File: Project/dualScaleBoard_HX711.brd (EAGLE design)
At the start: 75 x 14 mm, 44 parts, among them Q1 MMBT4403, Q2 MMBT4403, U1 HX711, U2 HX711

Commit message: BOM update
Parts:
- R7: value 20K -> 20k
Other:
- outline, holes or cut-outs redrawn

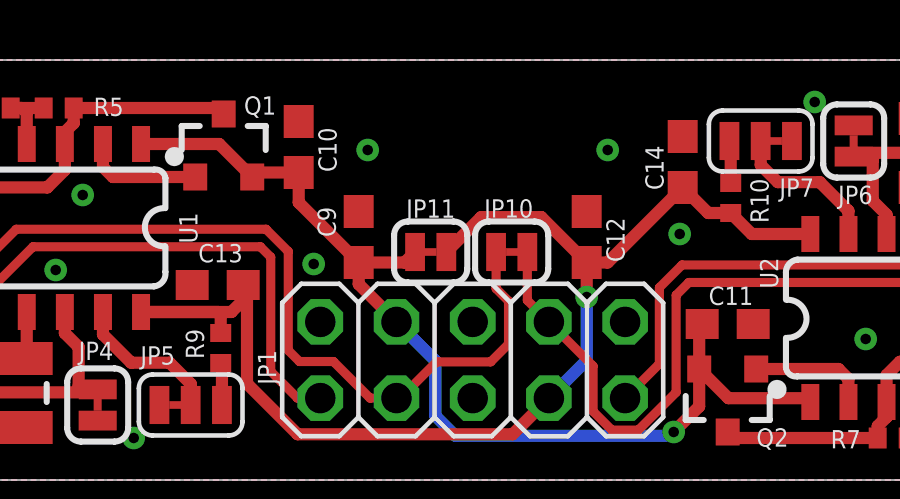
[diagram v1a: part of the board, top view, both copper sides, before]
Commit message: VDD LDO option
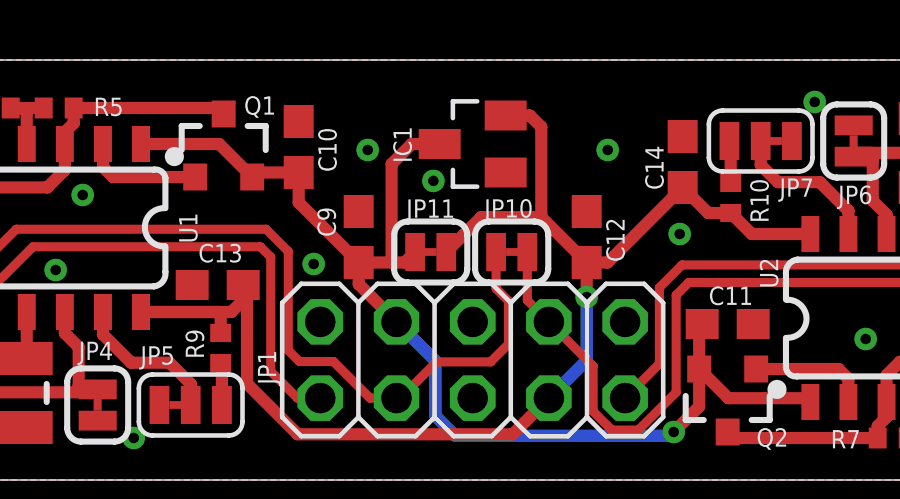
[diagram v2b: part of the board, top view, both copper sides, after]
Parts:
- added IC1: MCP1700T, linear:SOT23
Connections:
- net GND: now also IC1.1
- net VCC: now also IC1.3
- net VDD: now also IC1.2
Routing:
- net VCC: track 34.2 -> 39.4 mm
- net VDD: track 42.0 -> 46.3 mm
- net GND: vias 20 -> 21
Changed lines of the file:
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@@
 <element name="U$2" library="adafruit" library_urn="urn:adsk.eagle:library:420" package="FIDUCIAL_1MM" package3d_urn="urn:adsk.eagle:package:6240632/1" value="FIDUCIAL" x="62" y="12.5" smashed="yes"/>
 <element name="U$3" library="logo" library_urn="urn:adsk.eagle:library:264" package="ESD_10.00" value="" x="58.5" y="2.7" smashed="yes" rot="MR0"/>
+<element name="IC1" library="linear" library_urn="urn:adsk.eagle:library:262" package="SOT23" package3d_urn="urn:adsk.eagle:package:16489/2" value="MCP1700T" x="37.5" y="11.2" smashed="yes" rot="R90">
+<attribute name="LCSC" value="C39051" x="37.5" y="11.2" size="1.778" layer="27" rot="R90" display="off"/>
+<attribute name="NAME" x="35.468" y="10.565" size="0.6096" layer="25" rot="R90"/>
+<attribute name="POPULARITY" value="19" x="37.5" y="11.2" size="1.778" layer="27" rot="R90" display="off"/>
+<attribute name="VALUE" x="40.675" y="9.295" size="1.27" layer="27" rot="R90"/>
+</element>
 </elements>
 <signals>
@@
 <wire x1="29.85" y1="6.5" x2="29.977" y2="6.373" width="0.4064" layer="1"/>
 <wire x1="29.977" y1="6.373" x2="29.977" y2="3.21146875" width="0.4064" layer="1"/>
+<contactref element="IC1" pad="2"/>
+<wire x1="39.787" y1="11.771" x2="39.408" y2="12.15" width="0.4064" layer="1"/>
+<wire x1="38.6" y1="12.15" x2="39.408" y2="12.15" width="0.4064" layer="1"/>
+<wire x1="39.787" y1="11.771" x2="39.787" y2="8.763" width="0.4064" layer="1"/>
 </signal>
 <signal name="N$1">
@@
 <wire x1="31.7" y1="10.25" x2="31.7" y2="9.25" width="0.4064" layer="1"/>
 <wire x1="31.7" y1="9.25" x2="33.7" y2="7.25" width="0.4064" layer="1"/>
-<wire x1="33.7" y1="7.25" x2="35.2293" y2="7.25" width="0.4064" layer="1"/>
+<wire x1="33.7" y1="7.25" x2="34.798" y2="7.25" width="0.4064" layer="1"/>
+<wire x1="34.798" y1="7.25" x2="35.2293" y2="7.25" width="0.4064" layer="1"/>
 <wire x1="35.2293" y1="7.25" x2="35.5793" y2="7.6" width="0.4064" layer="1"/>
 <wire x1="36.2554" y1="3.9746" x2="34.96" y2="5.27" width="0.4064" layer="16"/>
@@
 <wire x1="45.15" y1="5.2" x2="45.05" y2="5.1" width="0.4064" layer="1"/>
 <wire x1="45.05" y1="5.1" x2="45.05" y2="3.7" width="0.4064" layer="1"/>
+<contactref element="IC1" pad="3"/>
+<wire x1="36.4" y1="11.2" x2="35.465" y2="11.2" width="0.4064" layer="1"/>
+<wire x1="35.465" y1="11.2" x2="34.798" y2="10.533" width="0.4064" layer="1"/>
+<wire x1="34.798" y1="10.533" x2="34.798" y2="7.25" width="0.4064" layer="1"/>
 </signal>
 <signal name="N$4">
@@
 <via x="34" y="11" extent="1-16" drill="0.35"/>
 <via x="42" y="11" extent="1-16" drill="0.35"/>
+<contactref element="IC1" pad="1"/>
+<via x="36.19" y="9.97" extent="1-16" drill="0.35"/>
 </signal>
 <signal name="N$23">

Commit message: pin reassignment
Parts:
- turned C12 to 270 degrees
- turned C13 to 0 degrees
- turned C9 to 270 degrees
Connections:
- net DOUT1: now also JP1.2
- net DOUT2: now also JP1.10
- net VCC: now also JP1.7; no longer JP1.4
- net VDD: now also JP1.4; no longer JP1.7
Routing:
- net VDD: track 46.3 -> 35.3 mm
- net SCK2: track 25.1 -> 20.9 mm
- net DOUT1: track 16.7 -> 19.2 mm
- net VCC: track 39.4 -> 40.1 mm
- net DOUT2: track 15.5 -> 16.0 mm
- net GND: vias 21 -> 23

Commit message: FPC version
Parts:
- removed JP1: (no value), pinhead:2X05
- removed JP10, JP11: (no value), SparkFun-Jumpers:SMT-JUMPER_2_NC_TRACE_SILK
- added J1: 687110149022, Wurth_Connectors_WR-FPC:687110149022
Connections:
- net DOUT1: now also J1.2; no longer JP1.1, JP1.2
- net DOUT2: now also J1.9; no longer JP1.10, JP1.9
- net GND: now also J1.1, J1.10, J1.5, J1.6, J1.Z1, J1.Z2; no longer JP1.5, JP1.6
- net SCK1: now also J1.4; no longer JP1.3, JP10.2
- net SCK2: now also J1.7; no longer JP1.8, JP10.1
- net VCC: now also J1.3, J1.8; no longer JP1.7, JP11.1
- net VDD: no longer JP1.4, JP11.2
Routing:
- net SCK1: track 28.3 -> 20.8 mm, vias 0 -> 2
- net VCC: track 40.1 -> 35.8 mm, vias 1 -> 2
- net DOUT1: track 19.2 -> 17.3 mm, vias 0 -> 2
- net DOUT2: track 16.0 -> 17.5 mm, vias 0 -> 2
- net VDD: track 35.3 -> 34.6 mm, vias 1 -> 2
- net SCK2: track 20.9 -> 21.1 mm, vias 0 -> 2
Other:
- board text added: "GND DOUT2 VCC SCK2 GND GND SCK1 VCC DOUT1 GND"
- board text removed: "C1"
- board text removed: "C2"
- board text removed: "D1"
- board text removed: "D2"
- board text removed: "GND"
- board text removed: "VCC"
- board text removed: "VDD"
